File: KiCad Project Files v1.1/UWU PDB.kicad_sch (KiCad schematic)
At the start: 65 parts, among them J1 XT90, J10 XT60 ESC, J11 PWM1, J12 PWM2, J13 PWM3, J14 PWM4, J15 PWM5, J16 PWM6, J17 PWM7, J18 PWM8, J19 XT90, J2 Conn_02x08_Odd_Even, J3 XT60 ESC, J4 XT60 ESC, J5 XT60 ESC, J6 XT60 ESC, J7 XT60 ESC, J8 XT60 ESC, J9 XT60 ESC

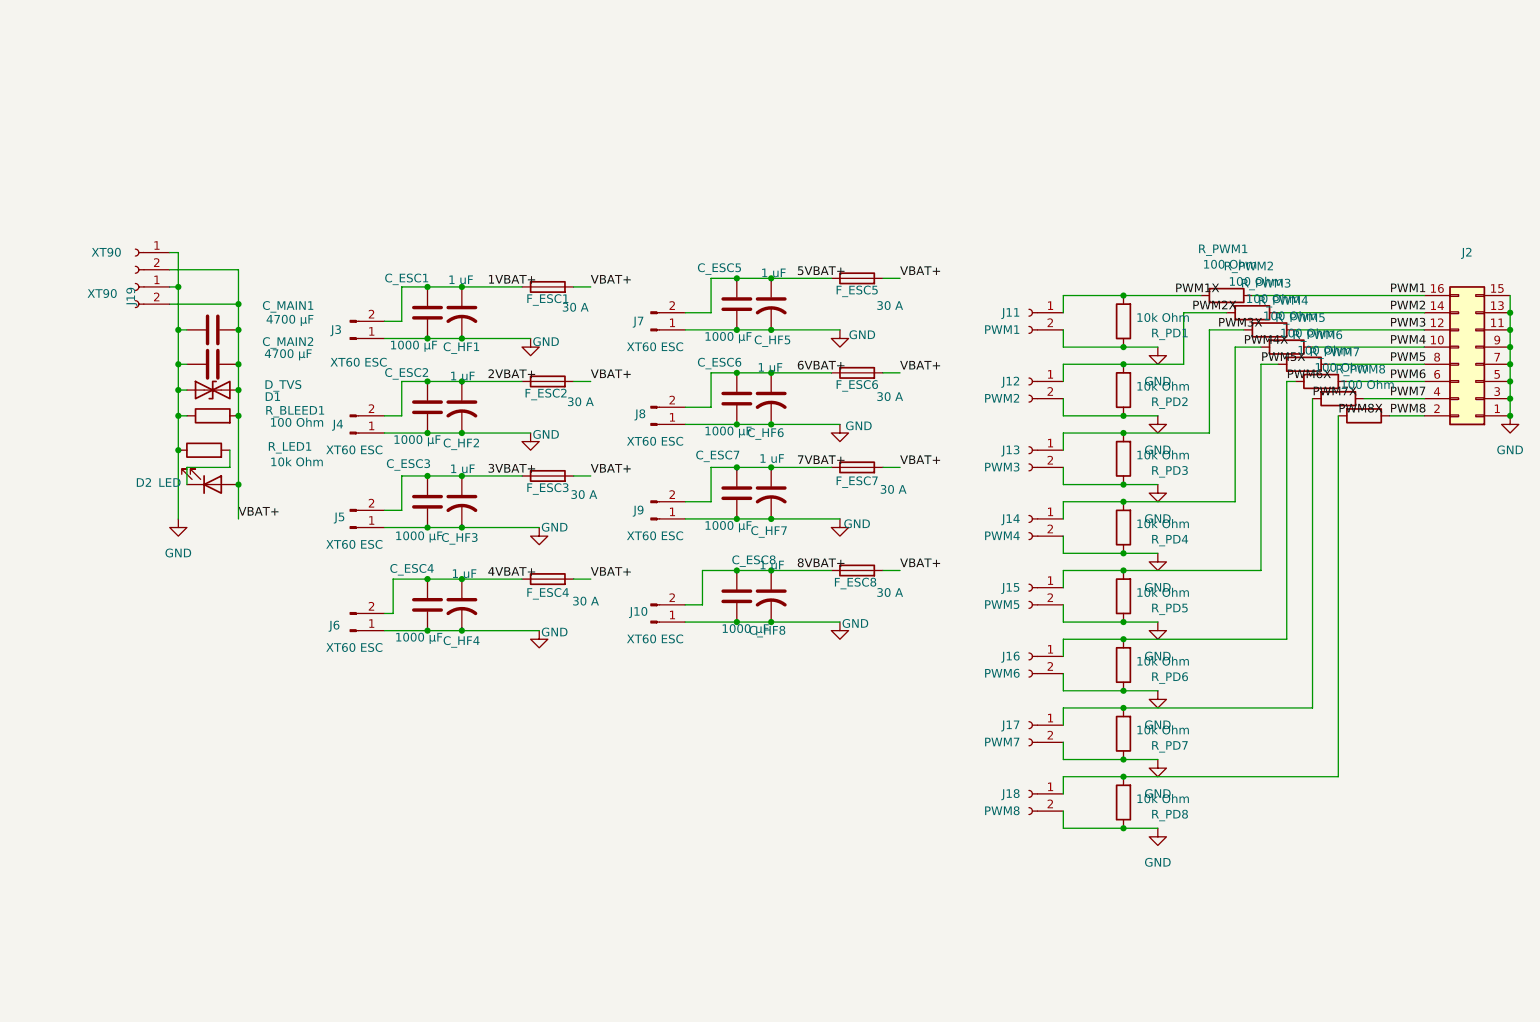
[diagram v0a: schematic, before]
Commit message: Update README, resolve R_BLEED1 value, add procurement BOMs
- Set R_BLEED1 to 22k Ohm (was stale 3.3k in schematic, README said 100 Ohm)
- Mark V1.1 known issues resolved in README
- Add Procurement section with LCSC/JLC sourcing notes and a
  still-need-to-source checklist
- Add SwimBladder_BOM_v1.1.csv (full reference BOM) and
  SwimBladder_LCSC_BatchBOM_v1.1.csv (LCSC batch-BOM upload, MOQ-adjusted
  for a 2-board build)
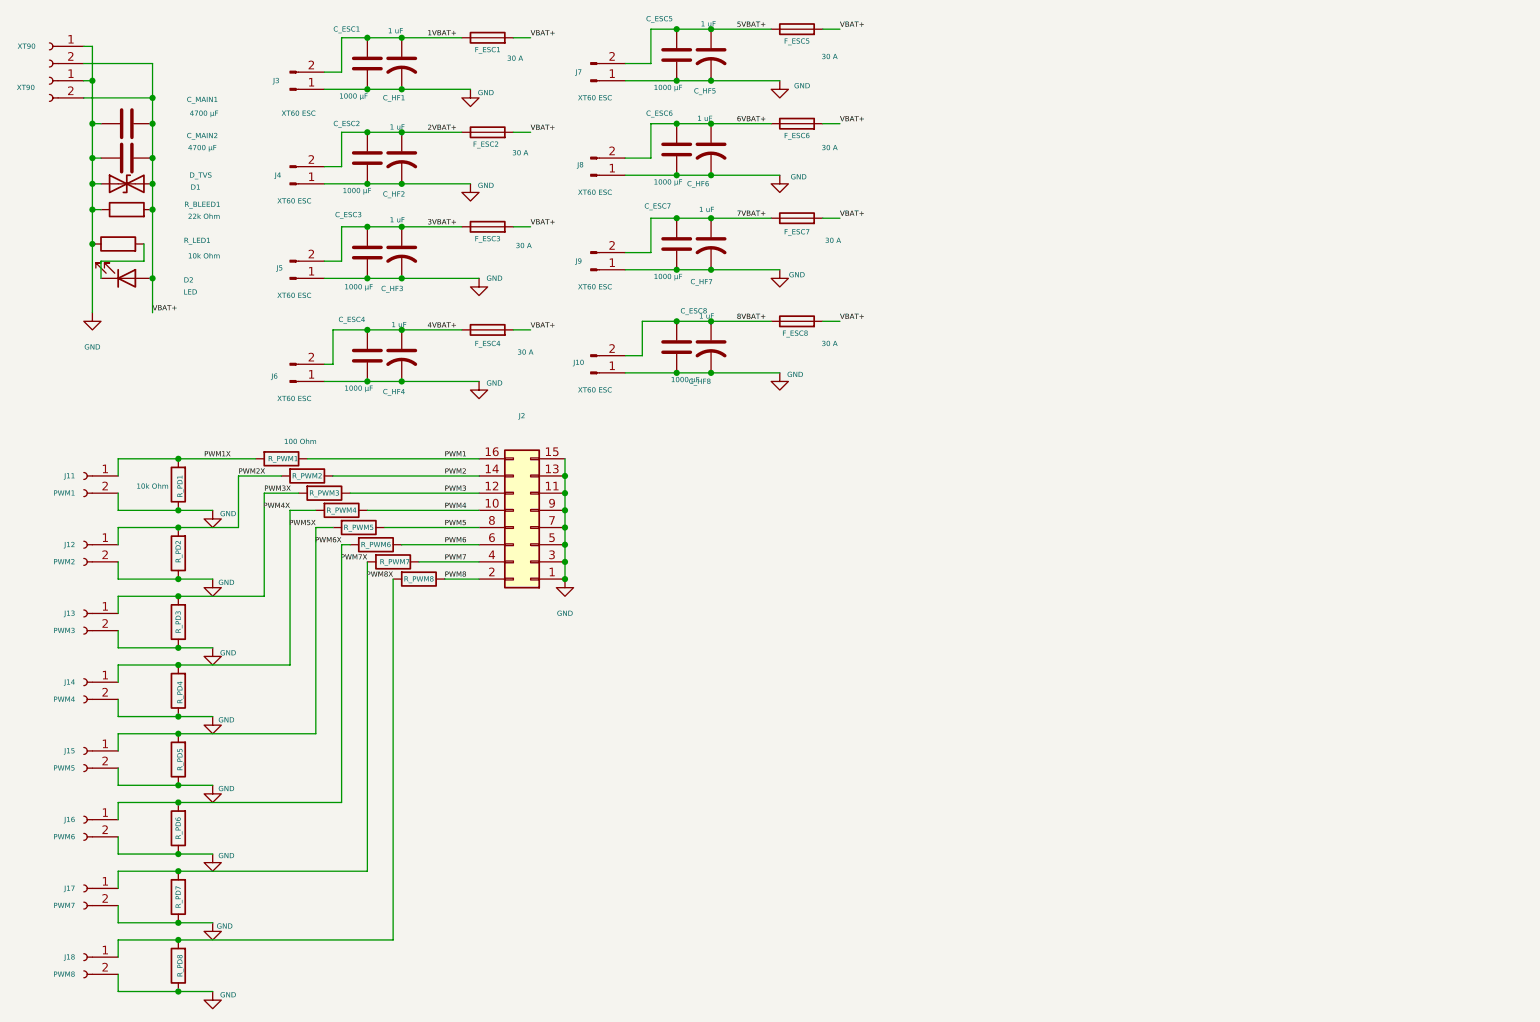
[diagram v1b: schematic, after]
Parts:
- D2: footprint LED_SMD:LED_1206_3216Metric -> LED_SMD:LED_0805_2012Metric
- R_BLEED1: value 100 Ohm -> 22k Ohm
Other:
- moved on the sheet: C_ESC1, C_ESC2, C_ESC3, C_ESC4, C_ESC5, C_ESC6, C_ESC7, C_ESC8, C_HF1, C_HF2, C_HF3, C_HF4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
